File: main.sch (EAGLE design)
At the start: 29 parts, among them IC1 MEGA88, IC2 AMS1117-5.0, Q1 32768Hz, Q2 BC817, Q3 IRF7473, SW1 EC12E_SW

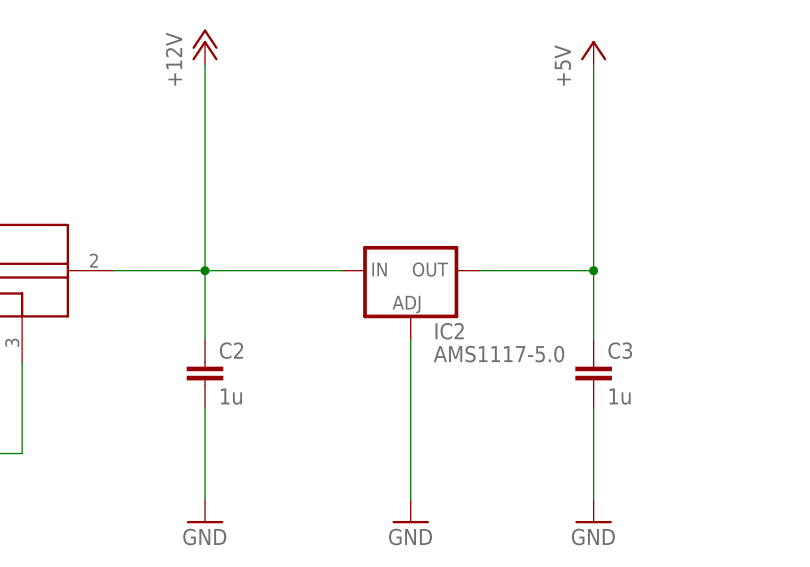
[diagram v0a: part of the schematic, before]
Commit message: Заменил AMS1117 на LM7805. От 12В AMS1117 сглючивает и сжигает атмегу
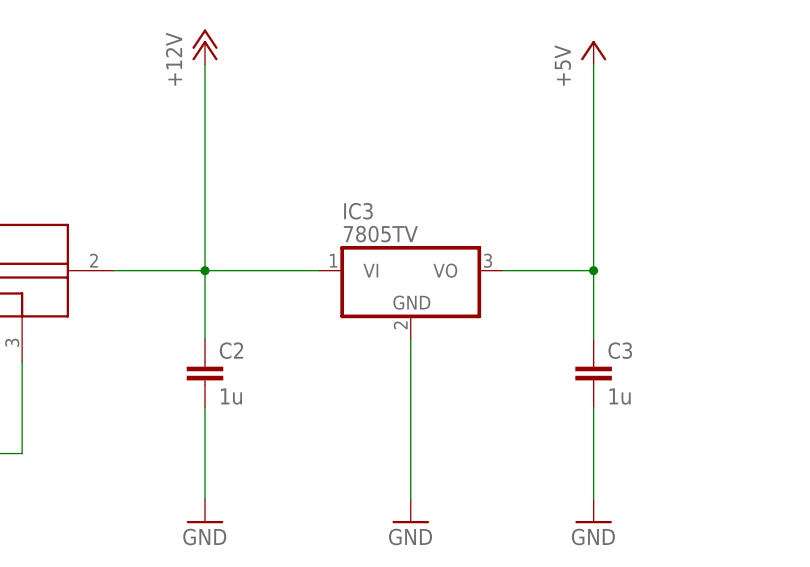
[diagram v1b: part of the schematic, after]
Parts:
- removed IC2: AMS1117-5.0, v-reg:LD117AS12TR
- added IC3: 7805TV, linear:7805TV
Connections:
- net +12V: now also IC3.VI; no longer IC2.IN
- net +5V: now also IC3.VO; no longer IC2.OUT
- net GND: now also IC3.GND; no longer IC2.ADJ
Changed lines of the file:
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@@
 <part name="R9" library="rcl" deviceset="R-EU_" device="R1206" value="10k"/>
 <part name="R10" library="rcl" deviceset="R-EU_" device="R1206" value="10k"/>
-<part name="IC2" library="v-reg" deviceset="LD117A?*" device="S" technology="12TR" value="AMS1117-5.0"/>
 <part name="P+9" library="supply1" deviceset="+12V" device=""/>
 <part name="P+2" library="supply1" deviceset="+5V" device=""/>
@@
 <part name="R14" library="rcl" deviceset="R-EU_" device="R1206" value="0"/>
 <part name="R15" library="rcl" deviceset="R-TRIMM" device="3296W"/>
+<part name="IC3" library="linear" deviceset="78*" device="TV" technology="05"/>
 </parts>
 <sheets>
@@
 <instance part="C2" gate="G$1" x="-63.5" y="53.34"/>
 <instance part="C3" gate="G$1" x="-20.32" y="53.34"/>
-<instance part="IC2" gate="G$1" x="-40.64" y="63.5"/>
 <instance part="P+9" gate="1" x="-63.5" y="88.9"/>
 <instance part="P+10" gate="1" x="-20.32" y="88.9"/>
@@
 <instance part="R14" gate="G$1" x="175.26" y="5.08" rot="R180"/>
 <instance part="R15" gate="G$1" x="213.36" y="22.86"/>
+<instance part="IC3" gate="A1" x="-40.64" y="63.5"/>
 </instances>
 <busses>
@@
 </segment>
 <segment>
-<pinref part="IC2" gate="G$1" pin="ADJ"/>
-<pinref part="GND13" gate="1" pin="GND"/>
-<wire x1="-40.64" y1="55.88" x2="-40.64" y2="38.1" width="0.1524" layer="91"/>
-</segment>
-<segment>
 <pinref part="C2" gate="G$1" pin="2"/>
 <pinref part="GND12" gate="1" pin="GND"/>
@@
 <wire x1="177.8" y1="33.02" x2="177.8" y2="35.56" width="0.1524" layer="91"/>
 <junction x="177.8" y="33.02"/>
+</segment>
+<segment>
+<pinref part="IC3" gate="A1" pin="GND"/>
+<pinref part="GND13" gate="1" pin="GND"/>
+<wire x1="-40.64" y1="55.88" x2="-40.64" y2="38.1" width="0.1524" layer="91"/>
 </segment>
 </net>
@@
 </segment>
 <segment>
-<pinref part="IC2" gate="G$1" pin="IN"/>
 <pinref part="P+9" gate="1" pin="+12V"/>
-<wire x1="-63.5" y1="63.5" x2="-48.26" y2="63.5" width="0.1524" layer="91"/>
 <wire x1="-63.5" y1="86.36" x2="-63.5" y2="63.5" width="0.1524" layer="91"/>
 <junction x="-63.5" y="63.5"/>
@@
 <pinref part="X2" gate="G$1" pin="3"/>
 <wire x1="-73.66" y1="63.5" x2="-63.5" y2="63.5" width="0.1524" layer="91"/>
+<pinref part="IC3" gate="A1" pin="VI"/>
+<wire x1="-50.8" y1="63.5" x2="-63.5" y2="63.5" width="0.1524" layer="91"/>
 </segment>
 </net>
@@
 </segment>
 <segment>
-<pinref part="IC2" gate="G$1" pin="OUT"/>
 <pinref part="C3" gate="G$1" pin="1"/>
-<wire x1="-33.02" y1="63.5" x2="-20.32" y2="63.5" width="0.1524" layer="91"/>
-<wire x1="-20.32" y1="63.5" x2="-20.32" y2="55.88" width="0.1524" layer="91"/>
 <pinref part="P+10" gate="1" pin="+5V"/>
+<wire x1="-20.32" y1="55.88" x2="-20.32" y2="63.5" width="0.1524" layer="91"/>
+<pinref part="IC3" gate="A1" pin="VO"/>
 <wire x1="-20.32" y1="63.5" x2="-20.32" y2="86.36" width="0.1524" layer="91"/>
+<wire x1="-30.48" y1="63.5" x2="-20.32" y2="63.5" width="0.1524" layer="91"/>
 <junction x="-20.32" y="63.5"/>
 </segment>

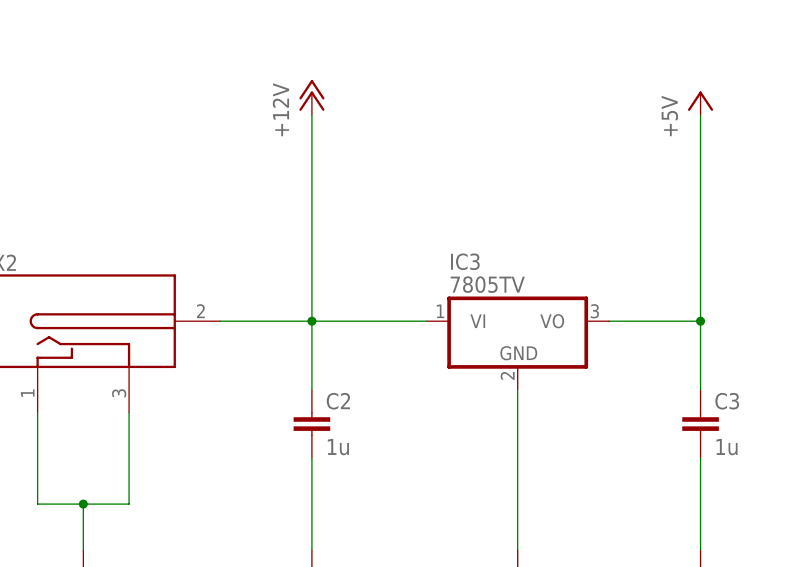
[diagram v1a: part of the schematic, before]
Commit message: Исправил ошибку на печатке, не была соединена земля LM7805 и земля Atmega о_О (орел жжет) Исправил печатку маски (правильно выводить tStop)
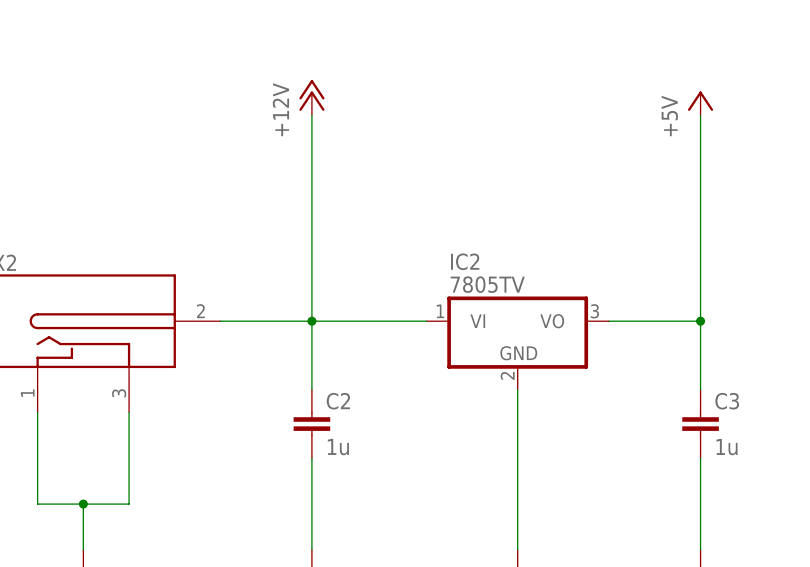
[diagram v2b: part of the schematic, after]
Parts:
- renumbered IC3 to IC2
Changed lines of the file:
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@@
 <part name="R14" library="rcl" deviceset="R-EU_" device="R1206" value="0"/>
 <part name="R15" library="rcl" deviceset="R-TRIMM" device="3296W"/>
-<part name="IC3" library="linear" deviceset="78*" device="TV" technology="05"/>
+<part name="IC2" library="linear" deviceset="78*" device="TV" technology="05"/>
 </parts>
 <sheets>
@@
 <instance part="R14" gate="G$1" x="175.26" y="5.08" rot="R180"/>
 <instance part="R15" gate="G$1" x="213.36" y="22.86"/>
-<instance part="IC3" gate="A1" x="-40.64" y="63.5"/>
+<instance part="IC2" gate="A1" x="-40.64" y="63.5"/>
 </instances>
 <busses>
@@
 </segment>
 <segment>
-<pinref part="IC3" gate="A1" pin="GND"/>
+<pinref part="IC2" gate="A1" pin="GND"/>
 <pinref part="GND13" gate="1" pin="GND"/>
 <wire x1="-40.64" y1="55.88" x2="-40.64" y2="38.1" width="0.1524" layer="91"/>
@@
 <pinref part="X2" gate="G$1" pin="3"/>
 <wire x1="-73.66" y1="63.5" x2="-63.5" y2="63.5" width="0.1524" layer="91"/>
-<pinref part="IC3" gate="A1" pin="VI"/>
-<wire x1="-50.8" y1="63.5" x2="-63.5" y2="63.5" width="0.1524" layer="91"/>
+<wire x1="-63.5" y1="63.5" x2="-50.8" y2="63.5" width="0.1524" layer="91"/>
+<pinref part="IC2" gate="A1" pin="VI"/>
 </segment>
 </net>
@@
 <pinref part="P+10" gate="1" pin="+5V"/>
 <wire x1="-20.32" y1="55.88" x2="-20.32" y2="63.5" width="0.1524" layer="91"/>
-<pinref part="IC3" gate="A1" pin="VO"/>
+<pinref part="IC2" gate="A1" pin="VO"/>
 <wire x1="-20.32" y1="63.5" x2="-20.32" y2="86.36" width="0.1524" layer="91"/>
 <wire x1="-30.48" y1="63.5" x2="-20.32" y2="63.5" width="0.1524" layer="91"/>
